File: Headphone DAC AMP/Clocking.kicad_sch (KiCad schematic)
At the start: 13 parts, among them Y1 Crystal_GND24, Y2 LMK6CE049152CDLFR, Y3 ASDLJ-E-45.1584MHz

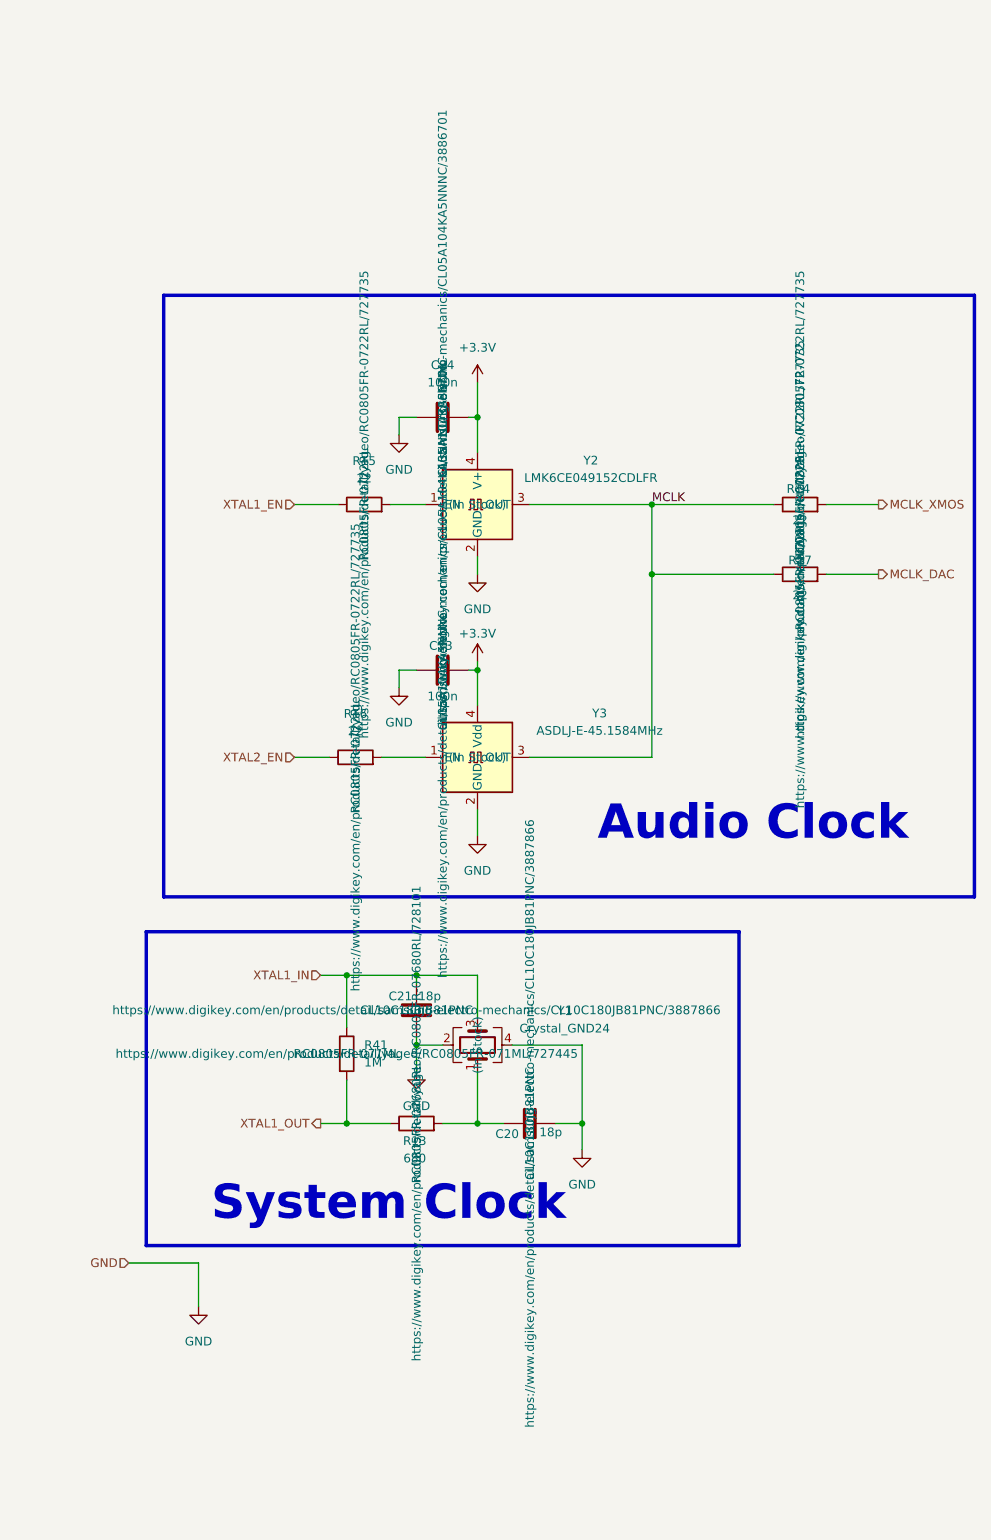
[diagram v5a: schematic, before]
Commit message: Worked on power schematic
planning to add debugging options
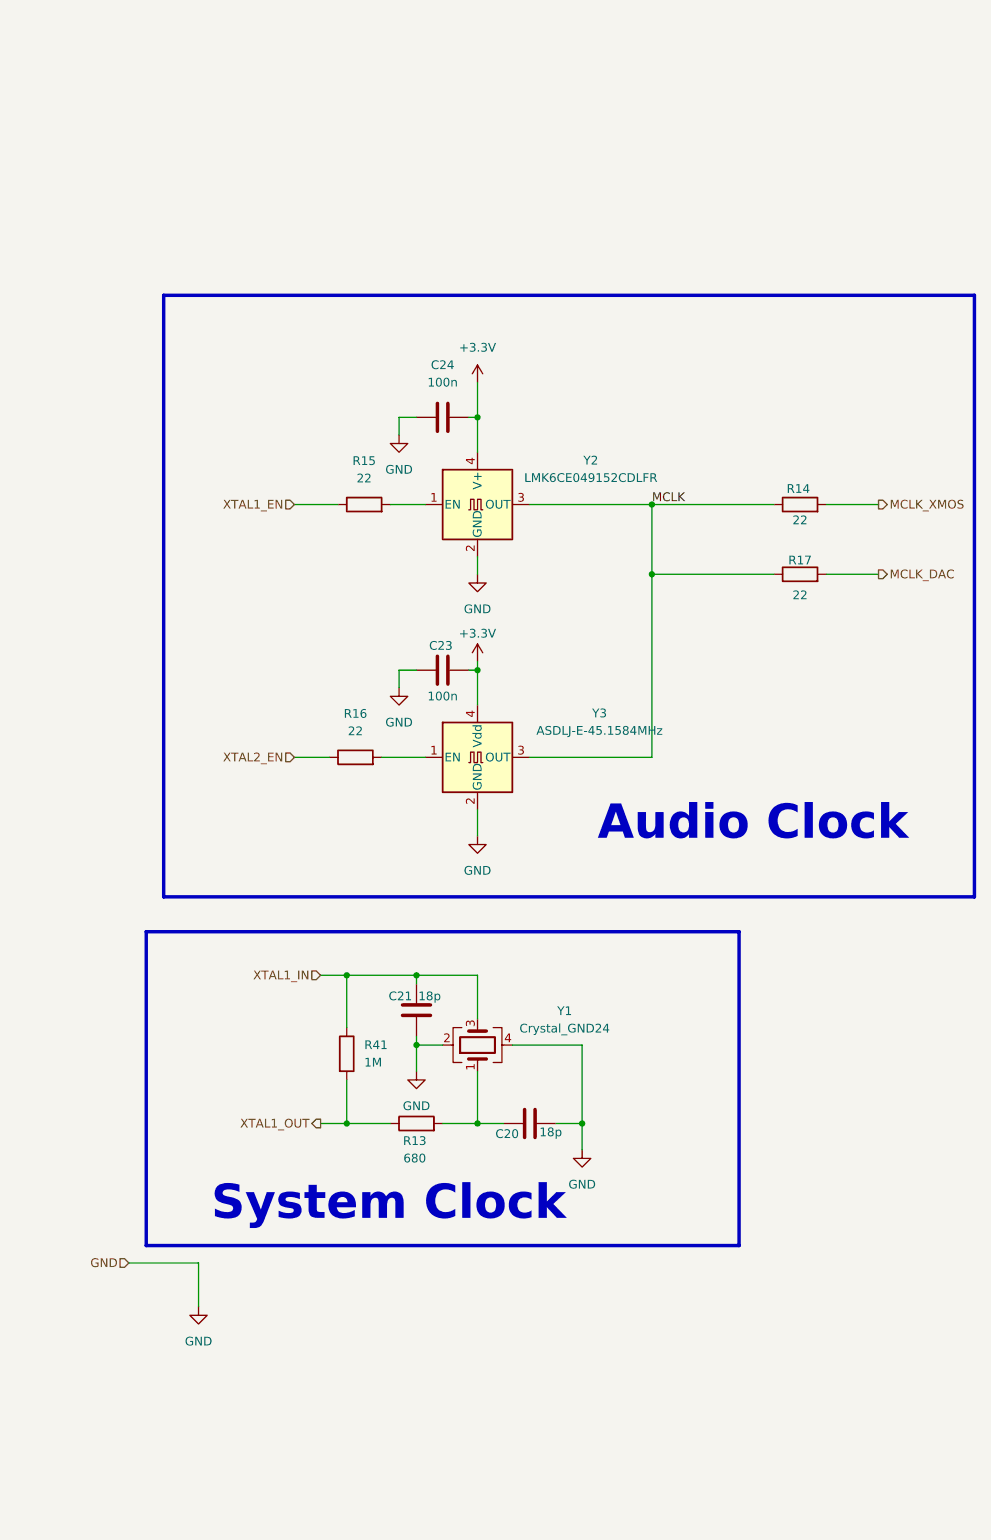
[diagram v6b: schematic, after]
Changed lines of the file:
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@@
 					(size 1.27 1.27)
 				)
+				(hide yes)
 			)
 		)
@@
 					(size 1.27 1.27)
 				)
+				(hide yes)
 			)
 		)
@@
 					(size 1.27 1.27)
 				)
+				(hide yes)
 			)
 		)
@@
 					(size 1.27 1.27)
 				)
+				(hide yes)
 			)
 		)
@@
 					(size 1.27 1.27)
 				)
+				(hide yes)
 			)
 		)
@@
 					(size 1.27 1.27)
 				)
+				(hide yes)
 			)
 		)
@@
 					(size 1.27 1.27)
 				)
+				(hide yes)
 			)
 		)
@@
 					(size 1.27 1.27)
 				)
+				(hide yes)
 			)
 		)
@@
 					(size 1.27 1.27)
 				)
+				(hide yes)
 			)
 		)
@@
 					(size 1.27 1.27)
 				)
+				(hide yes)
 			)
 		)
@@
 					(size 1.27 1.27)
 				)
+				(hide yes)
 			)
 		)
@@
 					(size 1.27 1.27)
 				)
+				(hide yes)
 			)
 		)
@@
 					(size 1.27 1.27)
 				)
+				(hide yes)
 			)
 		)
@@
 					(size 1.27 1.27)
 				)
+				(hide yes)
 			)
 		)
@@
 					(size 1.27 1.27)
 				)
+				(hide yes)
 			)
 		)
@@
 					(size 1.27 1.27)
 				)
+				(hide yes)
 			)
 		)
@@
 					(size 1.27 1.27)
 				)
+				(hide yes)
 			)
 		)
@@
 					(size 1.27 1.27)
 				)
+				(hide yes)
 			)
 		)
@@
 					(size 1.27 1.27)
 				)
+				(hide yes)
 			)
 		)
@@
 					(size 1.27 1.27)
 				)
+				(hide yes)
 			)
 		)
@@
 					(size 1.27 1.27)
 				)
+				(hide yes)
 			)
 		)
@@
 					(size 1.27 1.27)
 				)
+				(hide yes)
 			)
 		)
@@
 					(size 1.27 1.27)
 				)
-			)
-		)
+				(hide yes)
+			)
+		)

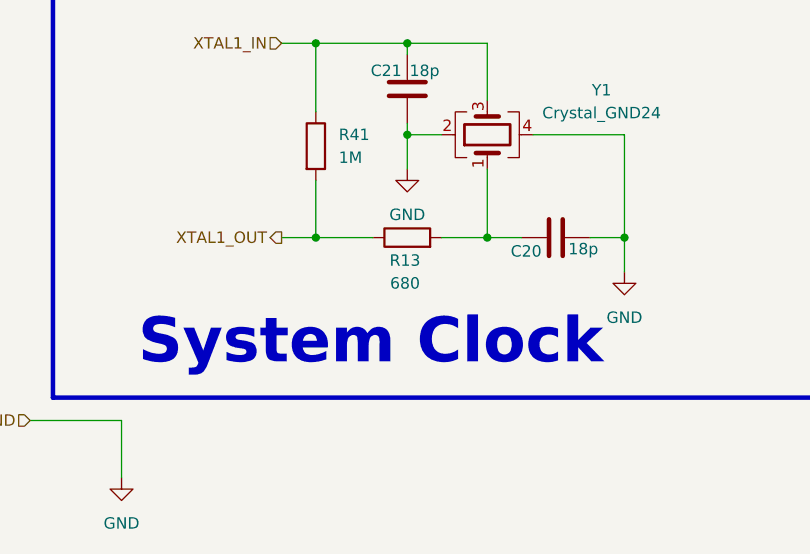
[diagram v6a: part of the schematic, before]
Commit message: Change resistor value in Clocking schematic to 220
Updated the value of a resistor in the Clocking.kicad_sch file from 680 to 220. Also updated the backup file to the latest version.
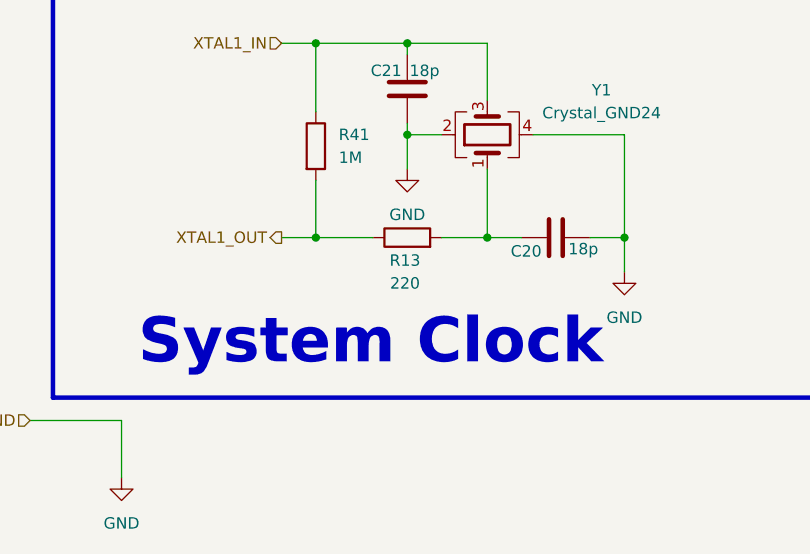
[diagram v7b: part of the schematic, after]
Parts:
- R13: value 680 -> 220
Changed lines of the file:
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@@
 			)
 		)
-		(property "Value" "680"
+		(property "Value" "220"
 			(at 88.646 143.51 90)
 			(effects
